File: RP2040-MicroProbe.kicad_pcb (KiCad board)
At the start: 4 copper layers, 50.8 x 25.4 mm, 66 parts, among them J1 CONN_MCU_JTAG, J10 CONN_USB, J2 CONN_MCU_UART, J3 CONN_DBG_COMB, J4 CONN_3V3_JUMPER, J7 CONN_DBG_JTAG, SW1 BOOTSEL, U1 W25Q128JVS, U2 RP2040, U3 74AUP1T17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

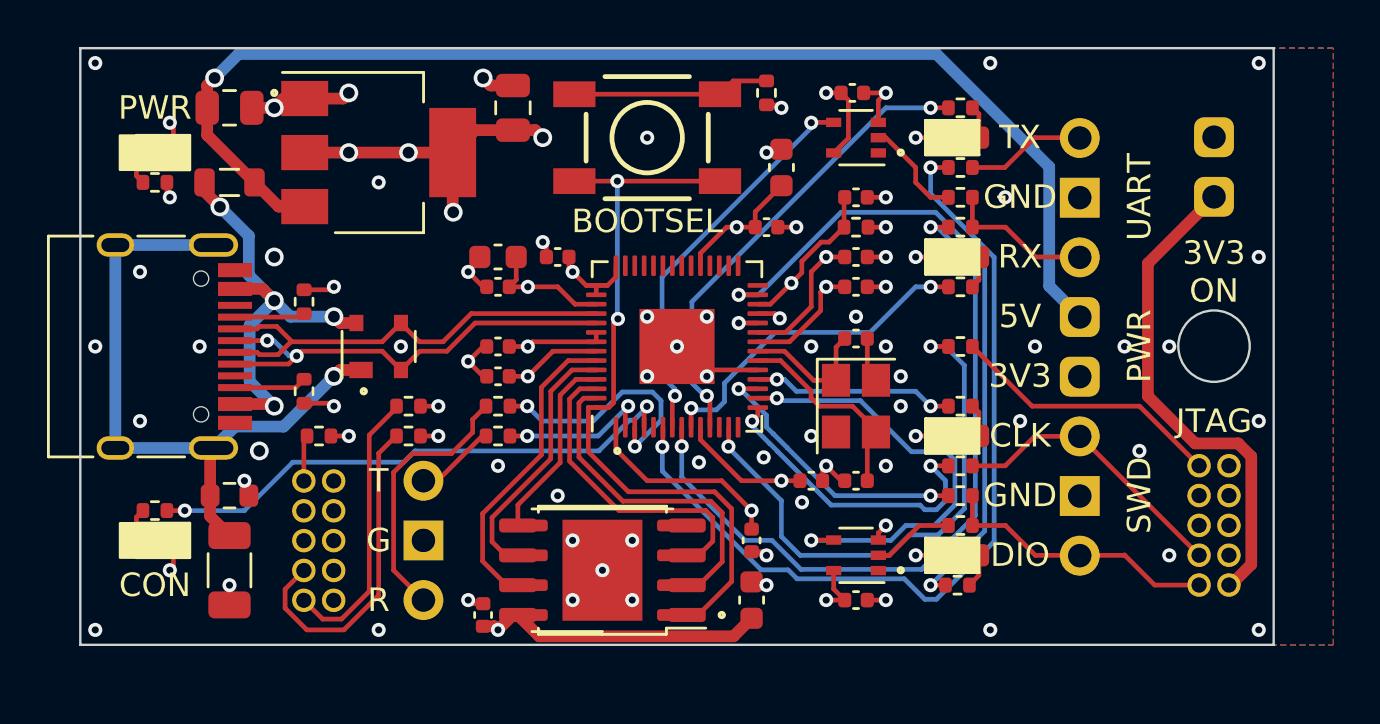
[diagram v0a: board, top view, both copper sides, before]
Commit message: Cleanup components a bit. Changed few components and footprints.
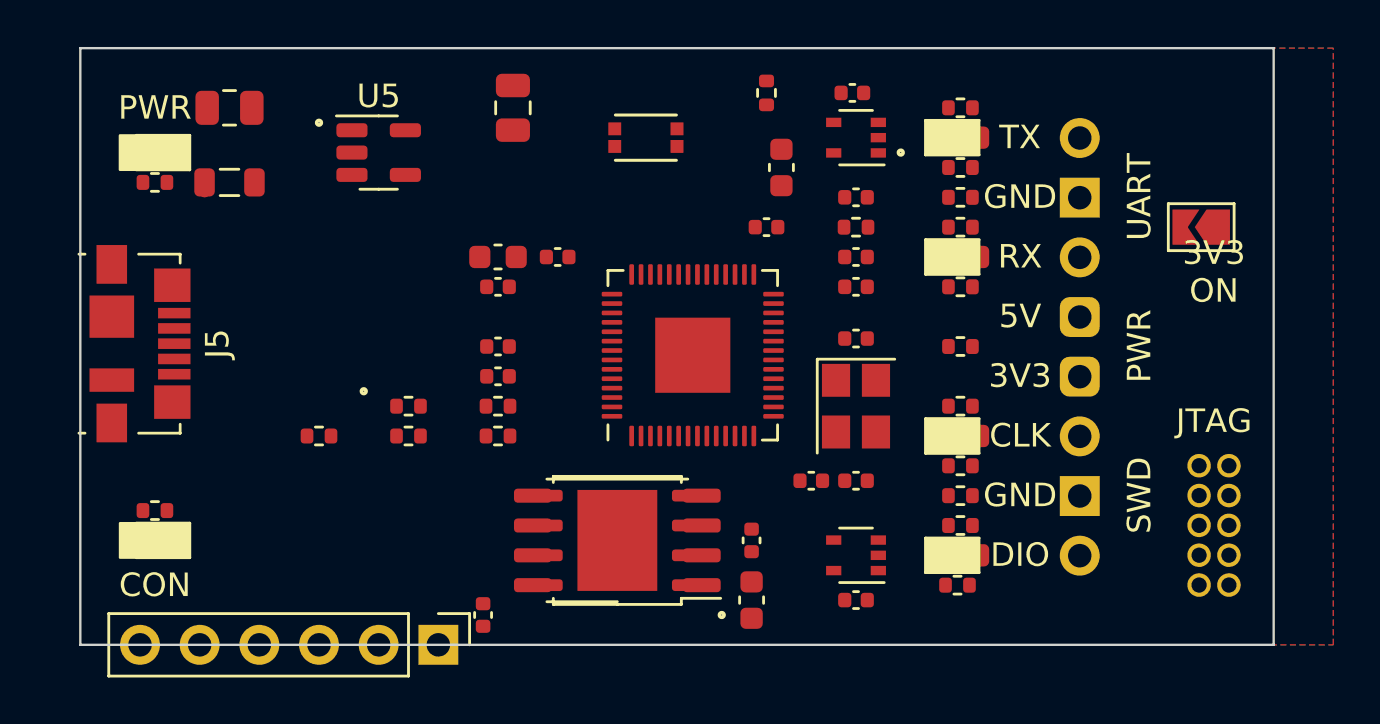
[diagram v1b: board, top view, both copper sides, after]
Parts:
- removed C21: 4.7nF 1kV, Capacitor_SMD:C_1206_3216Metric
- removed D3: PRTR5V0U2X, Package_TO_SOT_SMD:SOT-143
- removed J10: CONN_USB, Connector_USB:USB_C_Receptacle_HRO_TYPE-C-31-M-12
- removed J2: CONN_MCU_UART, Connector_PinHeader_2.54mm:PinHeader_1x03_P2.54mm_Vertical
- removed J4: CONN_3V3_JUMPER, Connector_PinHeader_2.54mm:PinHeader_1x02_P2.54mm_Vertical
- removed R10, R11: 5k1, Resistor_SMD:R_0402_1005Metric
- removed R12: 1M, Resistor_SMD:R_0603_1608Metric
- removed SW1: BOOTSEL, PCM_4ms_Switch:Button_Tact_Sqkg
- added J5: USB_B_Micro, Connector_USB:USB_Micro-B_Molex_47346-0001, F.Cu at (129.5, 107.8)
- added JP1: SJ_JTAG_3V3, Jumper:SolderJumper-2_P1.3mm_Open_TrianglePad1.0x1.5mm, F.Cu at (174.7, 102.9)
- added S1: BOOTSEL, lib:SW_EVPBB0AAB000, F.Cu at (151.1, 99.1)
- J1: value CONN_MCU_JTAG -> CONN_MCU_DEBUG; footprint Connector_PinHeader_1.27mm:PinHeader_2x05_P1.27mm_Vertical -> Connector_PinHeader_2.54mm:PinHeader_1x06_P2.54mm_Vertical
- U5: value AMS1117-3.3 -> MIC5205-3.3YM5; footprint Package_TO_SOT_SMD:SOT-223-3_TabPin2 -> Package_TO_SOT_SMD:SOT-23-5
- moved J1 4.84 mm to (142.2, 120.7), turned to -90 degrees
- moved U1 1.42 mm to (149.9, 116.2)
- moved U4 1.42 mm to (149.9, 116.2)
- moved U2 0.77 mm to (153.1, 108.3)
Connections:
- J1 pad 1: +3V3 -> HOST_TX
- J1 pad 2: HOST_DIO -> GND
- J1 pad 3: GND -> HOST_RX
- J1 pad 4: HOST_CLK -> HOST_RESET
- J1 pad 5: GND -> HOST_CLK
- J1 pad 6: unconnected-(J1-SWO/TDO-Pad6) -> HOST_DIO
- U5 pad 1: GND -> VUSB
- U5 pad 2: +3V3 -> GND
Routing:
- net +3V3: track 66.4 -> 0.00 mm, vias 15 -> 0
- net VUSB: track 52.8 -> 0.00 mm, vias 1 -> 0
- net GND: track 38.3 -> 1.13 mm, vias 76 -> 0
- net UART_TX: track 37.1 -> 0.00 mm, vias 2 -> 0
- net +1V1: track 32.7 -> 0.00 mm, vias 3 -> 0
- net QSPI_SS: track 31.5 -> 0.00 mm, vias 2 -> 0
- net UART_RX: track 31.2 -> 0.00 mm, vias 2 -> 0
- net LED_RUN: track 29.0 -> 0.00 mm, vias 2 -> 0
- net MCU_RESET: track 29.0 -> 0.00 mm, vias 2 -> 0
- net SHIELD: track 28.8 -> 0.00 mm, vias 1 -> 0
- net LED_ACT: track 23.2 -> 0.00 mm, vias 2 -> 0
- net DBG_RESET: track 23.2 -> 0.00 mm, vias 2 -> 0
- net MCU_CLK: track 22.5 -> 0.00 mm, vias 2 -> 0
- net TARGET_3V3: track 21.0 -> 0.07 mm
- net LED_TX: track 20.1 -> 0.00 mm, vias 2 -> 0
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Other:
- outline, holes or cut-outs redrawn
- board text removed: "G"
- board text removed: "R"
- board text removed: "T"

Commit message: Moved stuff around
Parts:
- removed R19, R20, R21, R22, R23: 100R, Resistor_SMD:R_0402_1005Metric
- moved R18 29.7 mm to (154.3, 135.9)
- moved C16 23.1 mm to (132.7, 115.4), turned to -90 degrees
- moved R7 19.6 mm to (148.0, 114.9), turned to 90 degrees
- moved R13 18.1 mm to (172.0, 132.1)
- moved D6 18.1 mm to (172.0, 128.3)
- moved R16 18.1 mm to (172.0, 130.8)
- moved R4 18.1 mm to (172.0, 127.0)
- moved R5 18.1 mm to (171.8, 134.6)
- moved D7 18.1 mm to (172.0, 133.3)
- moved R17 18.1 mm to (172.0, 129.5)
- moved S1 16.9 mm to (145.4, 114.9)
- moved C13 16.2 mm to (167.0, 133.3)
- moved U6 16.2 mm to (167.0, 131.4)
- moved D4 15.6 mm to (167.6, 83.8)
- moved R14 15.6 mm to (167.6, 87.6)
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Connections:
- C12 pad 1: MCU_RESET -> HOST_RESET
- R8 pad 1: MCU_RESET -> HOST_RESET
- U2 pad 2: MCU_TX -> HOST_TX
- U2 pad 24: MCU_CLK -> HOST_CLK
- U2 pad 25: MCU_DIO -> HOST_DIO
- U2 pad 26: MCU_RESET -> HOST_RESET
- U2 pad 3: MCU_RX -> HOST_RX
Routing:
- net GND: track 1.13 -> 0.00 mm
- net MCU_DIO: track 0.90 -> 0.00 mm
- net XOUT: track 0.00 -> 0.52 mm
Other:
- board size 50.8 x 25.4 mm -> 43.8 x 20.3 mm

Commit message: Moved stuff around
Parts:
- removed C3, C7: 100nF, Capacitor_SMD:C_0402_1005Metric
- removed J3: CONN_DBG_COMB, Connector_PinHeader_2.54mm:PinHeader_1x08_P2.54mm_Vertical
- removed R13, R14, R15, R16, R17, R18, R9: 100R, Resistor_SMD:R_0402_1005Metric
- added J2: CONN_DBG_COMB, Connector_PinSocket_2.54mm:PinSocket_1x07_P2.54mm_Vertical, F.Cu at (166.4, 100.3)
- added JP2: SJ_RESET, Jumper:SolderJumper-2_P1.3mm_Open_TrianglePad1.0x1.5mm, F.Cu at (153.0, 114.9)
- moved R5 23.0 mm to (161.2, 114.3)
- moved C13 22.4 mm to (157.5, 113.0)
- moved D7 20.7 mm to (161.3, 115.6)
- moved D6 20.2 mm to (161.3, 111.1)
- moved R2 20.1 mm to (161.3, 101.6)
- moved U6 19.1 mm to (157.5, 114.9)
- moved R4 18.1 mm to (161.3, 112.4)
- moved D4 17.7 mm to (161.3, 100.3)
- moved D1 17.1 mm to (161.3, 104.8)
- moved C17 16.7 mm to (157.5, 102.9)
- moved J7 16.2 mm to (156.9, 105.4), turned to 0 degrees
- moved R1 14.8 mm to (161.3, 103.5)
- moved JP1 14.1 mm to (153.0, 101.0)
- moved U3 13.0 mm to (157.5, 101.0)
- moved C12 12.1 mm to (153.0, 111.8)
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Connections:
- J7 pad 2: TARGET_DIO -> DBG_DIO
- J7 pad 4: TARGET_CLK -> DBG_CLK
- U2 pad 6: UART_TX -> TARGET_TX
- U2 pad 8: UART_RX -> TARGET_RX
- U3 pad 2: Net-(U3-A) -> TARGET_RX
- U6 pad 2: Net-(U6-A) -> DBG_DIO
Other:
- board size 43.8 x 20.3 mm -> 39.4 x 17.8 mm
- board text added: "BOOTSEL"
- board text removed: "3V3 ON"
- board text removed: "5V"
- board text removed: "JTAG"
- board text removed: "SWD"
- board text removed: "UART"

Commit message: Moved stuff around
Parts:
- J7: footprint Connector_PinHeader_1.27mm:PinHeader_2x05_P1.27mm_Vertical -> Connector_PinHeader_1.27mm:PinHeader_2x05_P1.27mm_Vertical_SMD
- moved R1 3.24 mm to (158.1, 102.9)
- moved J7 2.84 mm to (158.1, 108.0), turned to -90 degrees
- moved R4 2.62 mm to (158.8, 113.0)
- moved C17 1.91 mm to (155.6, 102.9), turned to 180 degrees
- moved D1 1.91 mm to (161.3, 102.9)
- moved D6 1.91 mm to (161.3, 113.0)
- moved C16 1.27 mm to (132.7, 114.9)
- moved C2 1.27 mm to (132.7, 112.4)
- moved C13 1.27 mm to (156.2, 113.0), turned to 180 degrees

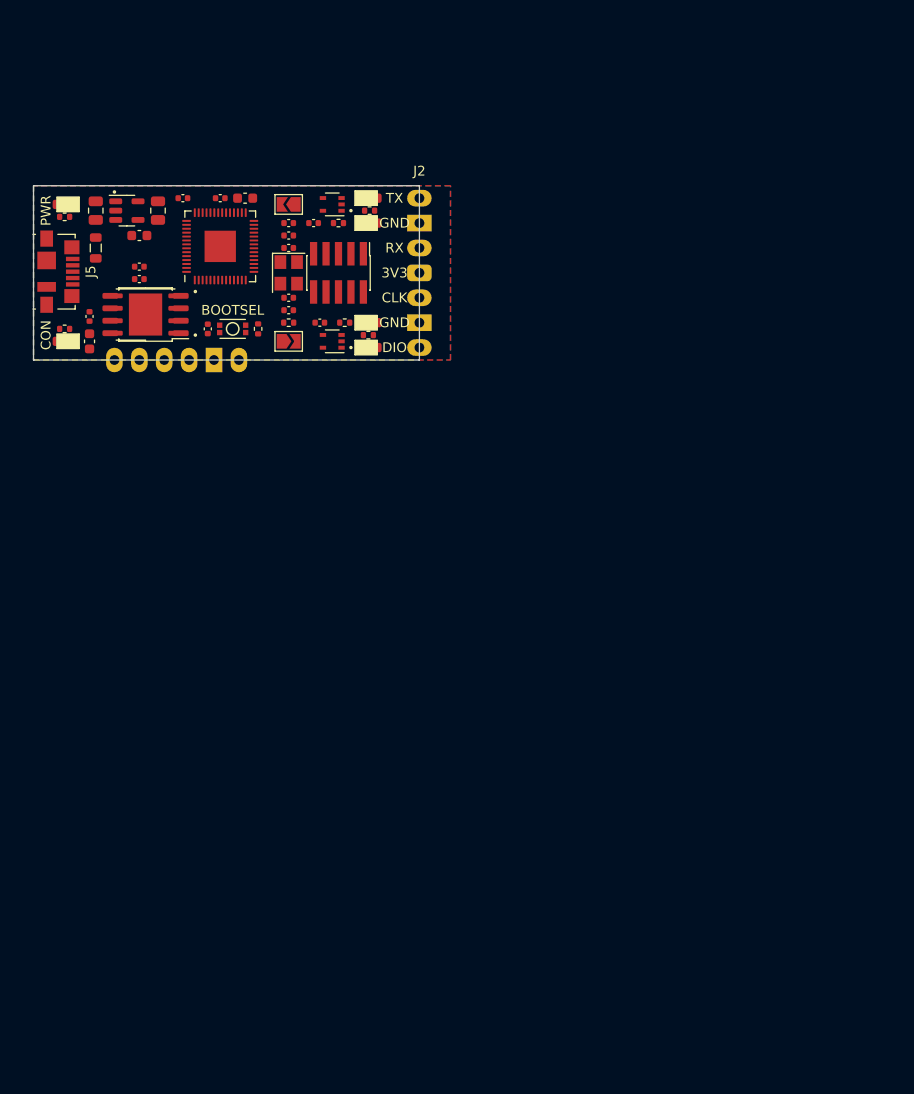
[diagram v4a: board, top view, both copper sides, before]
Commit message: Added traces and vias
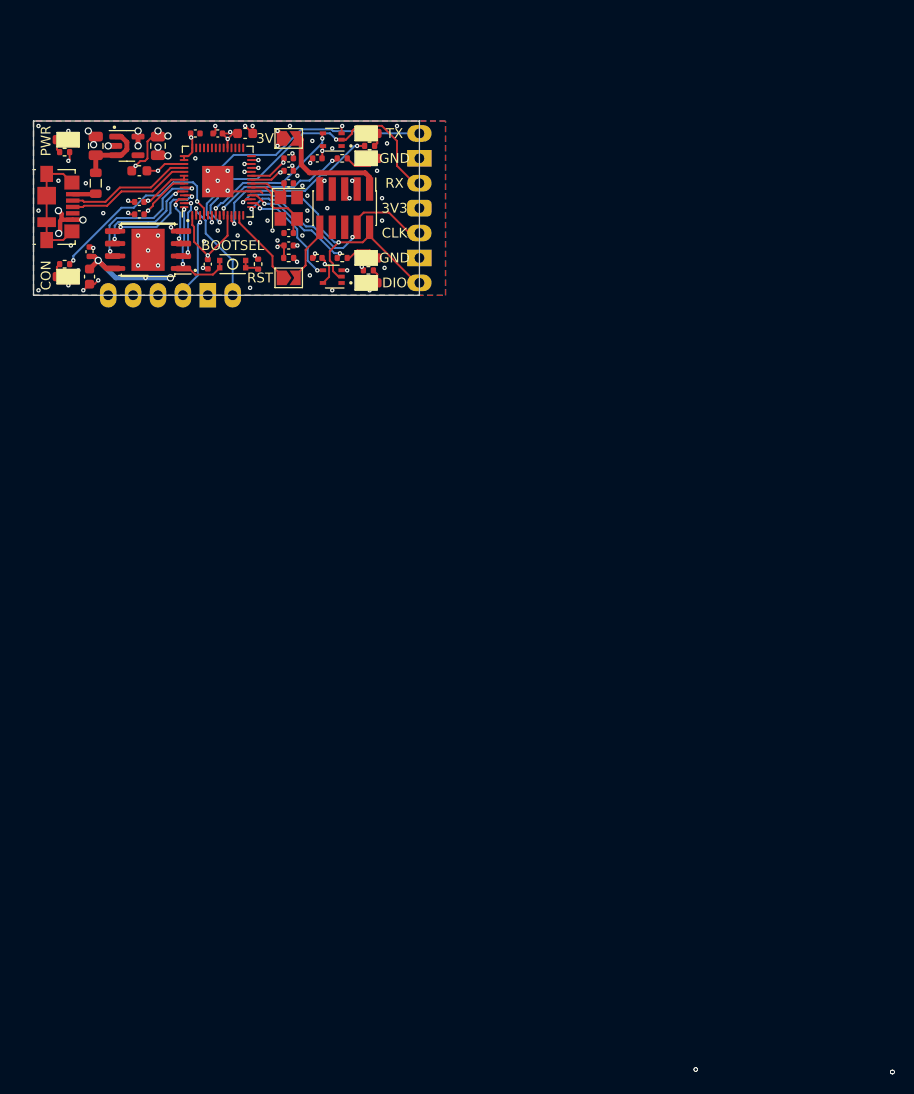
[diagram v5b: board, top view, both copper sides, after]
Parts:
- moved JP1 6.73 mm to (153.0, 94.2), turned to 0 degrees
- moved C6 6.73 mm to (143.5, 93.7), turned to 0 degrees
- moved J1 6.63 mm to (147.3, 110.2)
- moved J7 6.63 mm to (158.8, 101.3)
- moved C17 6.61 mm to (156.0, 96.3)
- moved R1 6.61 mm to (158.5, 96.3)
- moved C13 6.61 mm to (156.0, 106.4)
- moved C4 6.61 mm to (145.8, 93.7)
- moved U2 6.61 mm to (145.8, 98.6)
- moved R4 6.61 mm to (158.5, 106.4)
- moved U1 6.61 mm to (138.7, 105.6)
- moved U4 6.61 mm to (138.7, 105.6)
- moved C1 6.60 mm to (148.6, 93.7)
- moved C10 6.60 mm to (144.8, 107.1)
- moved C11 6.60 mm to (153.0, 97.5)
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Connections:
- JP1 pad 1: TARGET_3V3 -> +3V3
- JP1 pad 2: +3V3 -> TARGET_3V3
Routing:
- net +3V3: track 0.00 -> 50.4 mm, vias 0 -> 19
- net GND: track 0.00 -> 39.2 mm, vias 0 -> 82
- net TARGET_RX: track 0.00 -> 32.4 mm, vias 0 -> 2
- net +1V1: track 0.00 -> 32.4 mm, vias 0 -> 3
- net DBG_DIO: track 0.00 -> 30.5 mm, vias 0 -> 2
- net TARGET_TX: track 0.00 -> 29.4 mm, vias 0 -> 1
- net HOST_RESET: track 0.00 -> 28.5 mm, vias 0 -> 2
- net HOST_DIO: track 0.00 -> 25.4 mm, vias 0 -> 1
- net HOST_CLK: track 0.00 -> 23.1 mm, vias 0 -> 1
- net DBG_CLK: track 0.00 -> 23.0 mm, vias 0 -> 2
- net LED_ACT: track 0.00 -> 20.1 mm, vias 0 -> 2
- net LED_TX: track 0.00 -> 18.8 mm, vias 0 -> 2
- net LED_RUN: track 0.00 -> 17.3 mm, vias 0 -> 2
- net UART_RX_BUF: track 0.00 -> 15.4 mm, vias 0 -> 2
- net QSPI_SD3: track 0.00 -> 14.7 mm, vias 0 -> 2
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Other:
- board text added: "3V"
- board text added: "RST"

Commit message: Moved stuff around
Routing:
- net GND: track 39.2 -> 43.8 mm, vias 82 -> 84
- net +3V3: track 50.4 -> 52.4 mm
- net (no net): vias 6 -> 0
